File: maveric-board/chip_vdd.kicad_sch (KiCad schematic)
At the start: 17 parts, among them U3 Socket

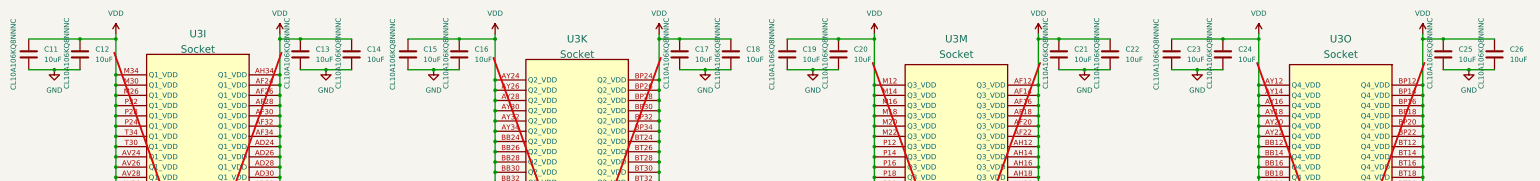
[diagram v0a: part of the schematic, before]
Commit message: swap some extended parts out for basic ones
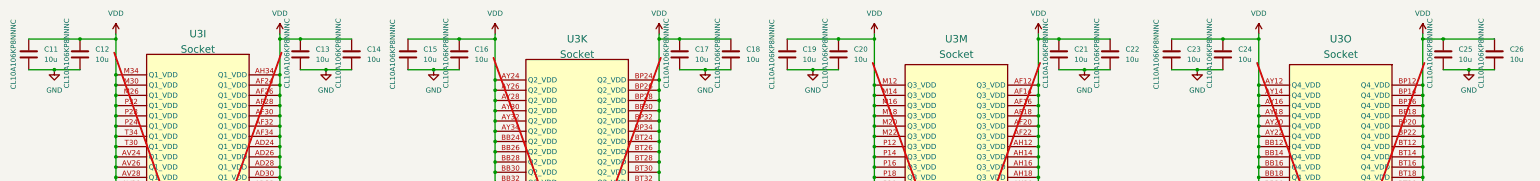
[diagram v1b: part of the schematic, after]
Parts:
- C11, C12, C13, C14, C15, C16, C17, C18, C19, C20, C21, C22, C23, C24, C25, C26: value 10uF -> 10u; JLCPCB Part # C95839 -> C19702; Mfr Part # CL10A106KQ8NNNC -> CL10A106KP8NNNC
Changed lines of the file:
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@@
 			)
 		)
-		(property "Value" "10uF"
+		(property "Value" "10u"
 			(at 22.86 30.4799 0)
 			(effects
@@
 			)
 		)
-		(property "JLCPCB Part #" "C95839"
+		(property "JLCPCB Part #" "C19702"
 			(at 19.05 29.21 0)
 			(effects
@@
 			)
 		)
-		(property "Mfr Part #" "CL10A106KQ8NNNC"
+		(property "Mfr Part #" "CL10A106KP8NNNC"
 			(at 15.24 29.21 90)
 			(effects
@@
 			)
 		)
-		(property "Value" "10uF"
+		(property "Value" "10u"
 			(at 184.15 30.4799 0)
 			(effects
@@
 			)
 		)
-		(property "JLCPCB Part #" "C95839"
+		(property "JLCPCB Part #" "C19702"
 			(at 180.34 29.21 0)
 			(effects
@@
 			)
 		)
-		(property "Mfr Part #" "CL10A106KQ8NNNC"
+		(property "Mfr Part #" "CL10A106KP8NNNC"
 			(at 177.038 28.956 90)
 			(effects
@@
 			)
 		)
-		(property "Value" "10uF"
+		(property "Value" "10u"
 			(at 102.87 30.4799 0)
 			(effects
@@
 			)
 		)
-		(property "JLCPCB Part #" "C95839"
+		(property "JLCPCB Part #" "C19702"
 			(at 99.06 29.21 0)
 			(effects
@@
 			)
 		)
-		(property "Mfr Part #" "CL10A106KQ8NNNC"
+		(property "Mfr Part #" "CL10A106KP8NNNC"
 			(at 95.758 28.956 90)
 			(effects
@@
 			)
 		)
-		(property "Value" "10uF"
+		(property "Value" "10u"
 			(at 306.07 30.4799 0)
 			(effects
@@
 			)
 		)
-		(property "JLCPCB Part #" "C95839"
+		(property "JLCPCB Part #" "C19702"
 			(at 302.26 29.21 0)
 			(effects
@@
 			)
 		)
-		(property "Mfr Part #" "CL10A106KQ8NNNC"
+		(property "Mfr Part #" "CL10A106KP8NNNC"
 			(at 298.45 29.21 90)
 			(effects
@@
 			)
 		)
-		(property "Value" "10uF"
+		(property "Value" "10u"
 			(at 129.54 30.4799 0)
 			(effects
@@
 			)
 		)
-		(property "JLCPCB Part #" "C95839"
+		(property "JLCPCB Part #" "C19702"
 			(at 125.73 29.21 0)
 			(effects
@@
 			)
 		)
-		(property "Mfr Part #" "CL10A106KQ8NNNC"
+		(property "Mfr Part #" "CL10A106KP8NNNC"
 			(at 122.428 28.956 90)
 			(effects
@@
 			)
 		)
-		(property "Value" "10uF"
+		(property "Value" "10u"
 			(at 223.52 30.4799 0)
 			(effects
@@
 			)
 		)
-		(property "JLCPCB Part #" "C95839"
+		(property "JLCPCB Part #" "C19702"
 			(at 219.71 29.21 0)
 			(effects
@@
 			)
 		)
-		(property "Mfr Part #" "CL10A106KQ8NNNC"
+		(property "Mfr Part #" "CL10A106KP8NNNC"
 			(at 216.408 28.956 90)
 			(effects
@@
 			)
 		)
-		(property "Value" "10uF"
+		(property "Value" "10u"
 			(at 386.08 30.4799 0)
 			(effects
@@
 			)
 		)
-		(property "JLCPCB Part #" "C95839"
+		(property "JLCPCB Part #" "C19702"
 			(at 382.27 29.21 0)
 			(effects
@@
 			)
 		)
-		(property "Mfr Part #" "CL10A106KQ8NNNC"
+		(property "Mfr Part #" "CL10A106KP8NNNC"
 			(at 378.968 28.956 90)
 			(effects
@@
 			)
 		)
-		(property "Value" "10uF"
+		(property "Value" "10u"
 			(at 373.38 30.4799 0)
 			(effects
@@
 			)
 		)
-		(property "JLCPCB Part #" "C95839"
+		(property "JLCPCB Part #" "C19702"
 			(at 369.57 29.21 0)
 			(effects
@@
 			)
 		)
-		(property "Mfr Part #" "CL10A106KQ8NNNC"
+		(property "Mfr Part #" "CL10A106KP8NNNC"
 			(at 366.268 28.956 90)
 			(effects
@@
 			)
 		)
-		(property "Value" "10uF"
+		(property "Value" "10u"
 			(at 90.17 30.4799 0)
 			(effects
@@
 			)
 		)
-		(property "JLCPCB Part #" "C95839"
+		(property "JLCPCB Part #" "C19702"
 			(at 86.36 29.21 0)
 			(effects
@@
 			)
 		)
-		(property "Mfr Part #" "CL10A106KQ8NNNC"
+		(property "Mfr Part #" "CL10A106KP8NNNC"
 			(at 83.058 28.956 90)
 			(effects
@@
 			)
 		)
-		(property "Value" "10uF"
+		(property "Value" "10u"
 			(at 278.13 30.4799 0)
 			(effects
@@
 			)
 		)
-		(property "JLCPCB Part #" "C95839"
+		(property "JLCPCB Part #" "C19702"
 			(at 274.32 29.21 0)
 			(effects
@@
 			)
 		)
-		(property "Mfr Part #" "CL10A106KQ8NNNC"
+		(property "Mfr Part #" "CL10A106KP8NNNC"
 			(at 271.018 28.956 90)
 			(effects
@@
 			)
 		)
-		(property "Value" "10uF"
+		(property "Value" "10u"
 			(at 290.83 30.4799 0)
 			(effects
@@
 			)
 		)
-		(property "JLCPCB Part #" "C95839"
+		(property "JLCPCB Part #" "C19702"
 			(at 287.02 29.21 0)
 			(effects
@@
 			)
 		)
-		(property "Mfr Part #" "CL10A106KQ8NNNC"
+		(property "Mfr Part #" "CL10A106KP8NNNC"
 			(at 283.718 28.956 90)
 			(effects
@@
 			)
 		)
-		(property "Value" "10uF"
+		(property "Value" "10u"
 			(at 116.84 30.4799 0)
 			(effects
@@
 			)
 		)
-		(property "JLCPCB Part #" "C95839"
+		(property "JLCPCB Part #" "C19702"
 			(at 113.03 29.21 0)
 			(effects
@@
 			)
 		)
-		(property "Mfr Part #" "CL10A106KQ8NNNC"
+		(property "Mfr Part #" "CL10A106KP8NNNC"
 			(at 109.22 29.21 90)
 			(effects
@@
 			)
 		)
-		(property "Value" "10uF"
+		(property "Value" "10u"
 			(at 210.82 30.4799 0)
 			(effects
@@
 			)
 		)
-		(property "JLCPCB Part #" "C95839"
+		(property "JLCPCB Part #" "C19702"
 			(at 207.01 29.21 0)
 			(effects
@@
 			)
 		)
-		(property "Mfr Part #" "CL10A106KQ8NNNC"
+		(property "Mfr Part #" "CL10A106KP8NNNC"
 			(at 203.2 29.21 90)
 			(effects
@@
 			)
 		)
-		(property "Value" "10uF"
+		(property "Value" "10u"
 			(at 196.85 30.4799 0)
 			(effects
@@
 			)
 		)
-		(property "JLCPCB Part #" "C95839"
+		(property "JLCPCB Part #" "C19702"
 			(at 193.04 29.21 0)
 			(effects
@@
 			)
 		)
-		(property "Mfr Part #" "CL10A106KQ8NNNC"
+		(property "Mfr Part #" "CL10A106KP8NNNC"
 			(at 189.738 28.956 90)
 			(effects
@@
 			)
 		)
-		(property "Value" "10uF"
+		(property "Value" "10u"
 			(at 35.56 30.4799 0)
 			(effects
@@
 			)
 		)
-		(property "JLCPCB Part #" "C95839"
+		(property "JLCPCB Part #" "C19702"
 			(at 31.75 29.21 0)
 			(effects
@@
 			)
 		)
-		(property "Mfr Part #" "CL10A106KQ8NNNC"
+		(property "Mfr Part #" "CL10A106KP8NNNC"
 			(at 28.448 28.956 90)
 			(effects
@@
 			)
 		)
-		(property "Value" "10uF"
+		(property "Value" "10u"
 			(at 318.77 30.4799 0)
 			(effects
@@
 			)
 		)
-		(property "JLCPCB Part #" "C95839"
+		(property "JLCPCB Part #" "C19702"
 			(at 314.96 29.21 0)
 			(effects
@@
 			)
 		)
-		(property "Mfr Part #" "CL10A106KQ8NNNC"
+		(property "Mfr Part #" "CL10A106KP8NNNC"
 			(at 311.658 28.956 90)
 			(effects

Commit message: resync all symbols to schematic, reannotate schematic
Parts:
- renumbered C11 to C12, C12 to C13, C13 to C14, C14 to C15, C15 to C16, C16 to C17, C17 to C18, C18 to C19, C19 to C20, C20 to C21, C21 to C22, C22 to C23, C23 to C24, C24 to C25, C25 to C26, C26 to C27

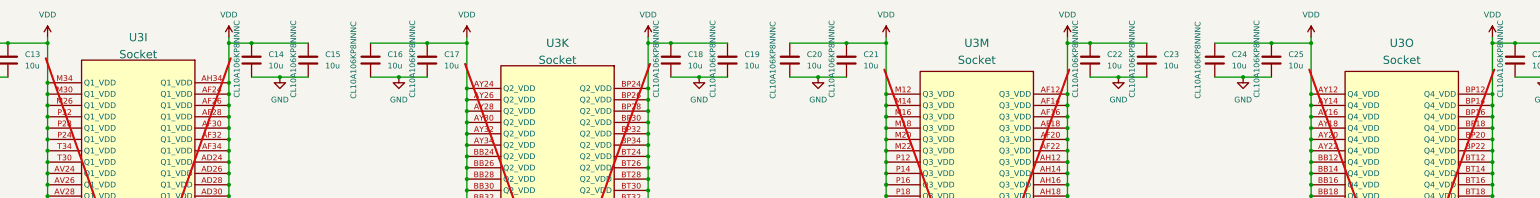
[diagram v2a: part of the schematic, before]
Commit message: fixup schematic + redo banana jack footprints to match jlc render
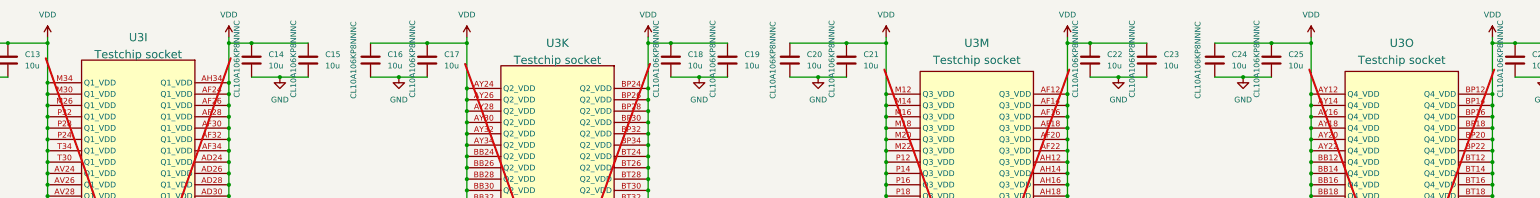
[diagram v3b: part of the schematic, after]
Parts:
- U3: value Socket -> Testchip socket
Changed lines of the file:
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@@
 			)
 		)
-		(property "Value" "Socket"
+		(property "Value" "Testchip socket"
 			(at 60.96 27.94 0)
 			(effects
@@
 			)
 		)
-		(property "Value" "Socket"
+		(property "Value" "Testchip socket"
 			(at 154.94 29.21 0)
 			(effects
@@
 			)
 		)
-		(property "Value" "Socket"
+		(property "Value" "Testchip socket"
 			(at 344.17 29.21 0)
 			(effects
@@
 			)
 		)
-		(property "Value" "Socket"
+		(property "Value" "Testchip socket"
 			(at 248.92 29.21 0)
 			(effects
